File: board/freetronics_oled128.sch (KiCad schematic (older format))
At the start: 42 parts, among them IC1 TPS61040, P1 CONN_10, P2 MICROSD, Q1 2N7002, Q2 2N7002

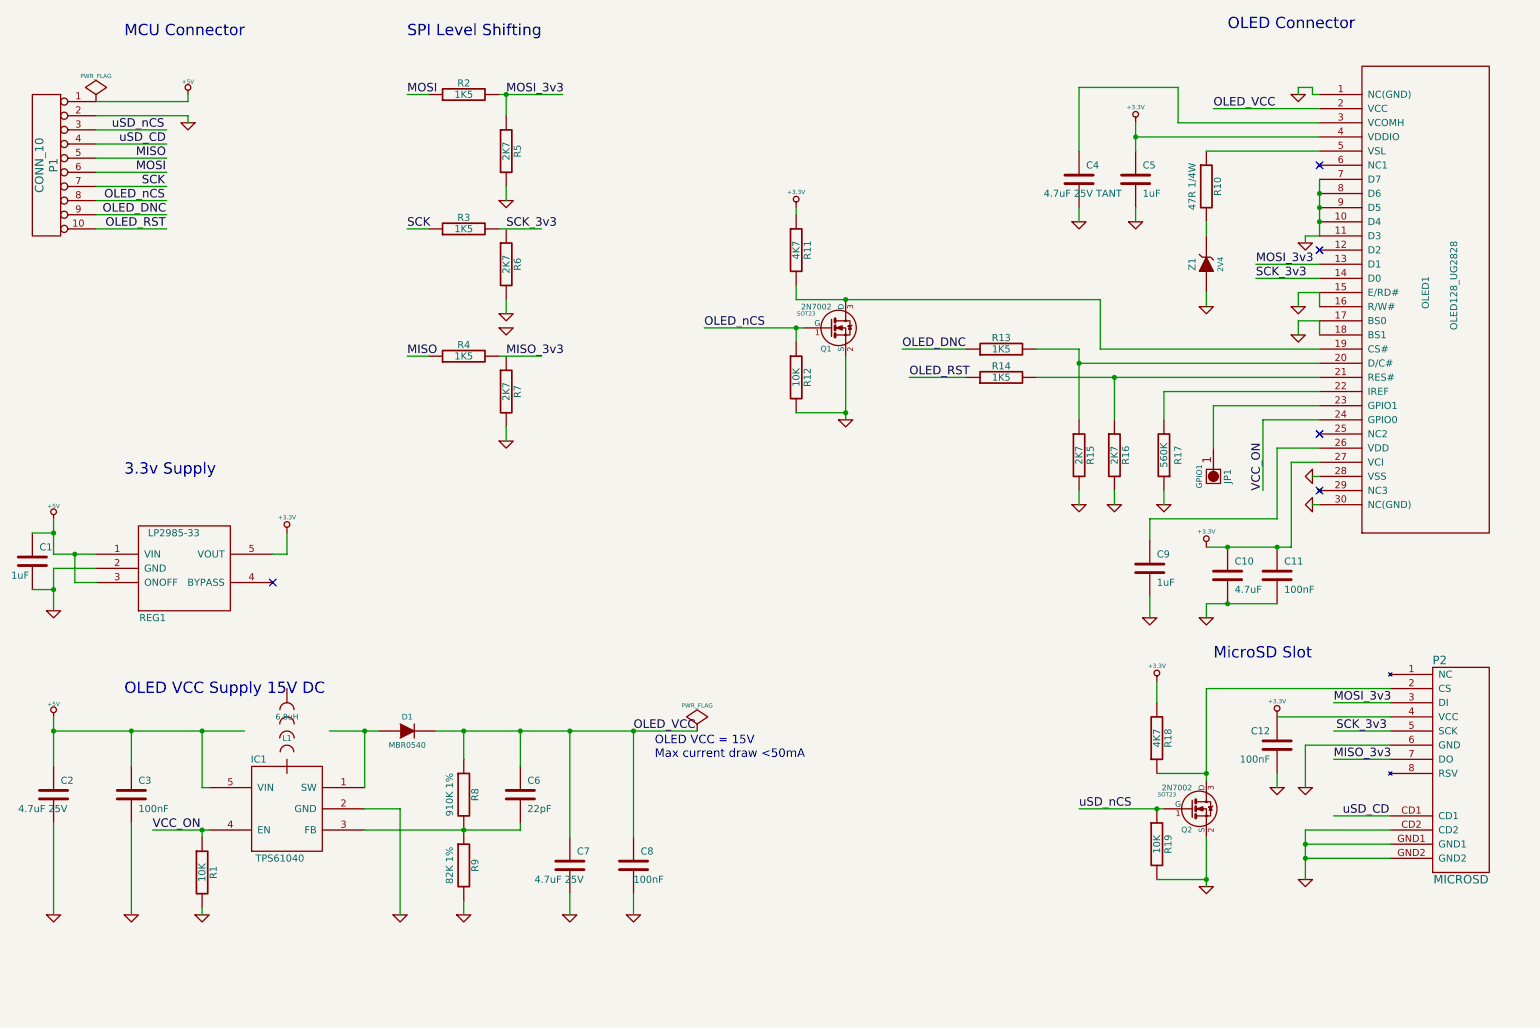
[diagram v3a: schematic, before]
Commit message: Replace ambiguous diode footprint
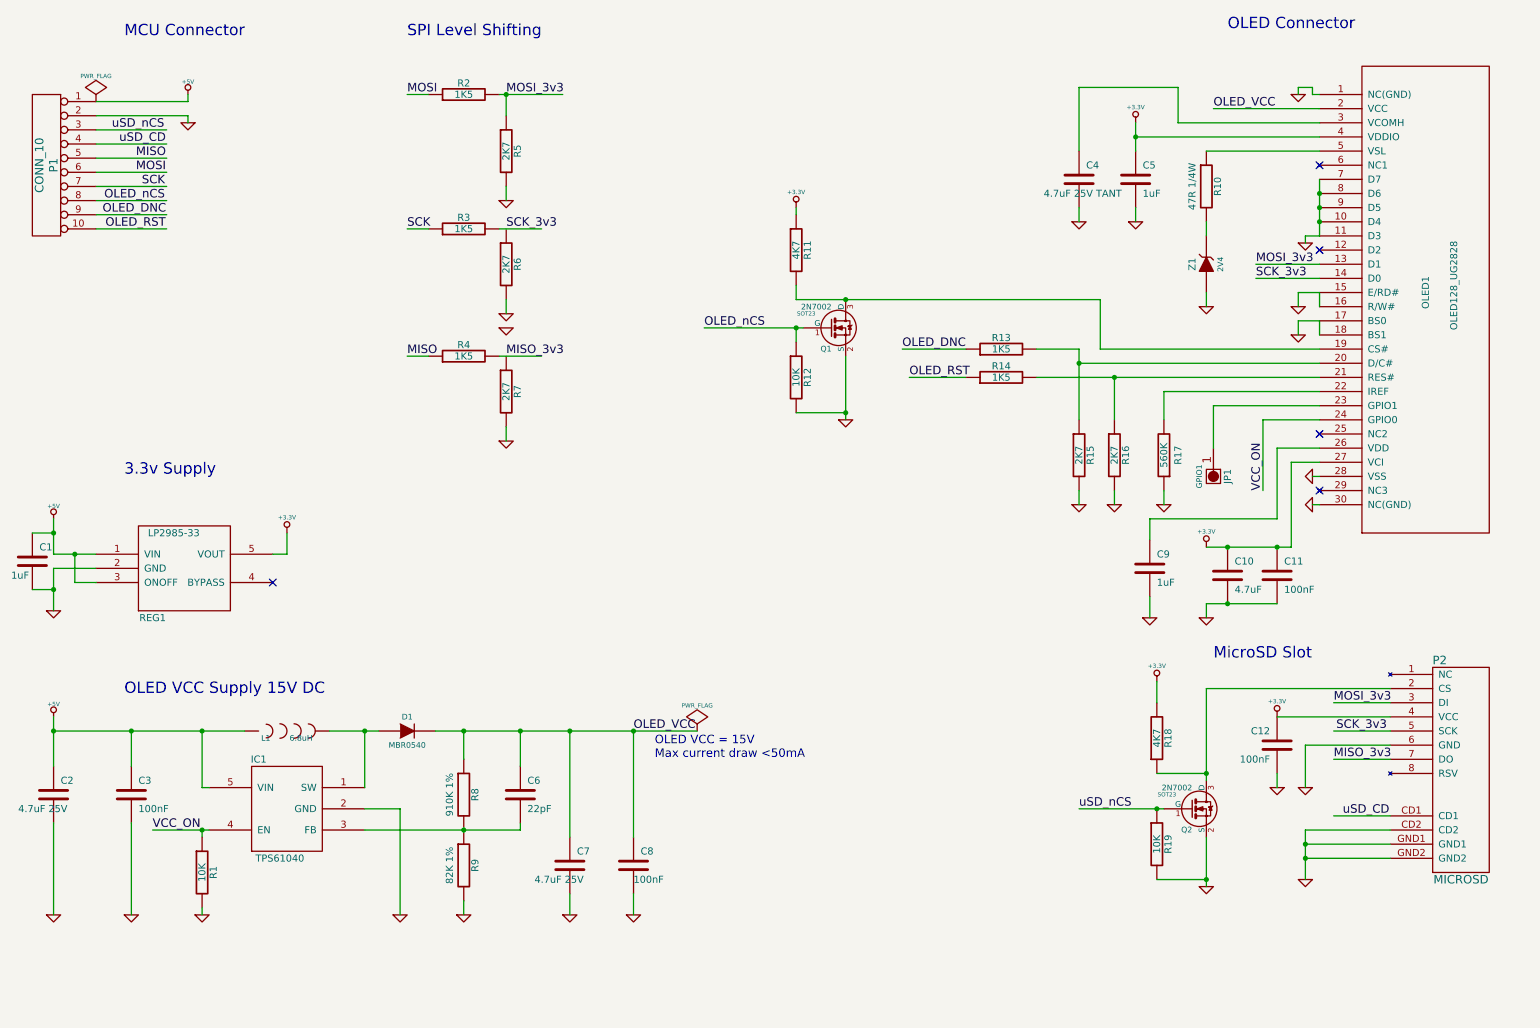
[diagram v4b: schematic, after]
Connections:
- wire segments 170 -> 139
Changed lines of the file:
@@
-EESchema Schematic File Version 2  date Thu 28 Feb 2013 12:36:34 EST
+EESchema Schematic File Version 2  date Tue 19 Mar 2013 09:15:38 EST
+LIBS:freetronics_kicad_sch_lib
 LIBS:power
 LIBS:device
@@
 LIBS:contrib
 LIBS:valves
-LIBS:freetronics_kicad_sch_lib
 LIBS:freetronics_oled128-cache
 EELAYER 25  0
@@
 Sheet 1 1
 Title "Freetronics OLED128              http://www.freetronics.com/oled128"
-Date "28 feb 2013"
+Date "18 mar 2013"
 Rev "0.9"
 Comp "(C)2013 Freetronics Pty Ltd"
@@
 Comment4 ""
 $EndDescr
+$Comp
+L DIODE D1
+U 1 1 514791C6
+P 3250 5650
+F 0 "D1" H 3250 5750 40  0000 C CNN
+F 1 "MBR0540" H 3250 5550 40  0000 C CNN
+	1    3250 5650
+	1    0    0    -1
+$EndComp
 Connection ~ 8250 3150
 Connection ~ 6350 2600
 Wire Wire Line
-	8150 2600 6350 2600
-Wire Wire Line
-	6350 2600 6000 2600
+	8150 2600 6000 2600
 Wire Wire Line
 	6000 2000 6000 1950
@@
 	8700 1350 9700 1350
 Wire Wire Line
-	8400 1350 8400 1450
-Wire Wire Line
-	8400 1450 8400 1550
+	8400 1350 8400 1550
 Connection ~ 8400 1450
 Wire Wire Line
@@
 	6000 2600 6000 2500
 Wire Wire Line
-	6350 3000 6350 3400
-Wire Wire Line
-	6350 3400 6350 3450
+	6350 3000 6350 3450
 Wire Wire Line
 	9700 3250 8600 3250
@@
 	9400 4150 8500 4150
 Wire Wire Line
-	8900 4750 8900 4850
+	8900 4850 8900 4750
 Connection ~ 9400 4350
 Wire Wire Line
 	8500 4700 8500 4850
 Wire Wire Line
-	8900 6000 8900 5950
-Wire Wire Line
-	8900 5950 8900 5350
-Wire Wire Line
-	750  4400 750  4250
-Wire Wire Line
-	750  4250 750  4150
+	8900 6000 8900 5350
+Wire Wire Line
+	750  4150 750  4400
 Connection ~ 8550 6200
 Wire Wire Line
 	1550 1400 1050 1400
 Wire Wire Line
-	8600 6200 8550 6200
-Wire Wire Line
-	8550 6200 8000 6200
+	8600 6200 8000 6200
 Connection ~ 9600 6550
 Wire Wire Line
-	9600 6550 10200 6550
+	10200 6550 9600 6550
 Wire Wire Line
 	9800 6250 10200 6250
@@
 	8550 6700 8900 6700
 Wire Wire Line
-	8900 6400 8900 6700
-Wire Wire Line
-	8900 6700 8900 6750
+	8900 6400 8900 6750
 Connection ~ 8900 6700
 Wire Wire Line
@@
 	9250 2450 9700 2450
 Wire Wire Line
-	4350 1150 3950 1150
-Wire Wire Line
-	3950 1150 3900 1150
+	4350 1150 3900 1150
 Wire Wire Line
 	3950 1300 3950 1150
@@
 	600  4250 750  4250
 Wire Wire Line
-	750  4500 1050 4500
+	1050 4500 750  4500
 Connection ~ 1800 6350
 Wire Wire Line
-	1850 6350 1800 6350
-Wire Wire Line
-	1800 6350 1450 6350
+	1850 6350 1450 6350
 Wire Wire Line
 	1800 6900 1800 6950
 Wire Wire Line
-	750  5900 750  5650
-Wire Wire Line
-	750  5650 750  5550
+	750  5900 750  5550
 Wire Wire Line
 	1300 6300 1300 6950
@@
 	3650 5850 3650 5650
 Wire Wire Line
-	2100 5650 1800 5650
-Wire Wire Line
-	1800 5650 1300 5650
-Wire Wire Line
-	1300 5650 750  5650
+	2100 5650 750  5650
 Connection ~ 3650 6350
 Wire Wire Line
-	4050 6350 4050 6300
+	4050 6300 4050 6350
 Connection ~ 4400 5650
 Wire Wire Line
@@
 	2950 6200 3200 6200
 Wire Wire Line
-	2700 5650 2950 5650
-Wire Wire Line
-	2950 5650 3050 5650
+	2700 5650 3050 5650
 Connection ~ 750  5650
 Wire Wire Line
@@
 	8900 2050 8900 2150
 Wire Wire Line
-	9700 1750 9700 1850
-Wire Wire Line
-	9700 1850 9700 1950
-Wire Wire Line
-	9700 1950 9700 2050
-Wire Wire Line
-	9700 2050 9700 2150
+	9700 1750 9700 2150
 Connection ~ 9700 2050
 Wire Wire Line
@@
 Connection ~ 4850 5650
 Wire Wire Line
-	3450 5650 3650 5650
-Wire Wire Line
-	3650 5650 4050 5650
-Wire Wire Line
-	4050 5650 4400 5650
-Wire Wire Line
-	4400 5650 4850 5650
-Wire Wire Line
-	4850 5650 5300 5650
-Wire Wire Line
-	2950 6350 3650 6350
-Wire Wire Line
-	3650 6350 4050 6350
+	3450 5650 5300 5650
+Wire Wire Line
+	4050 6350 2950 6350
 Wire Wire Line
 	4050 5650 4050 5900
@@
 	1800 6400 1800 6350
 Wire Wire Line
-	900  4600 900  4400
+	900  4400 900  4600
 Wire Wire Line
 	900  4600 1050 4600
 Connection ~ 900  4400
 Wire Wire Line
-	750  4800 750  4650
-Wire Wire Line
-	750  4650 750  4500
+	750  4500 750  4800
 Wire Wire Line
 	600  4650 750  4650
@@
 	8900 5350 10200 5350
 Wire Wire Line
-	9600 6350 10200 6350
-Wire Wire Line
-	9600 6700 9600 6550
-Wire Wire Line
-	9600 6550 9600 6450
-Wire Wire Line
-	9600 6450 9600 6350
+	10200 6350 9600 6350
+Wire Wire Line
+	9600 6350 9600 6700
 Wire Wire Line
 	9600 6450 10200 6450
@@
 	1550 2100 1050 2100
 Wire Wire Line
-	1050 4400 900  4400
-Wire Wire Line
-	900  4400 750  4400
+	750  4400 1050 4400
 Wire Wire Line
 	8550 5300 8550 5450
 Wire Wire Line
-	9500 4350 9500 3750
-Wire Wire Line
-	8900 4350 9050 4350
-Wire Wire Line
-	9050 4350 9400 4350
-Wire Wire Line
-	9400 4350 9500 4350
+	9500 3750 9500 4350
+Wire Wire Line
+	9500 4350 8900 4350
 Connection ~ 9050 4350
 Wire Wire Line
-	9400 4750 9050 4750
-Wire Wire Line
-	9050 4750 8900 4750
+	8900 4750 9400 4750
 Connection ~ 9050 4750
 Wire Wire Line
@@
 	8600 3250 8600 3450
 Wire Wire Line
-	9700 3150 8250 3150
-Wire Wire Line
-	8250 3150 7700 3150
+	9700 3150 7700 3150
 Wire Wire Line
 	8250 3150 8250 3450
@@
 	9700 3050 8000 3050
 Wire Wire Line
-	8000 2950 7700 2950
-Wire Wire Line
-	8000 3450 8000 3050
-Wire Wire Line
-	8000 3050 8000 2950
+	7700 2950 8000 2950
+Wire Wire Line
+	8000 2950 8000 3450
 Connection ~ 6350 3400
 Wire Wire Line
@@
 Connection ~ 6000 2800
 Wire Wire Line
-	5350 2800 6000 2800
-Wire Wire Line
-	6000 2800 6050 2800
+	5350 2800 6050 2800
 Wire Wire Line
 	2300 4400 2400 4400
@@
 $EndComp
 $Comp
-L DIODE D1
-U 1 1 511C32E9
-P 3250 5650
-F 0 "D1" H 3250 5750 40  0000 C CNN
-F 1 "MBR0540" H 3250 5550 40  0000 C CNN
-	1    3250 5650
-	1    0    0    -1
-$EndComp
-$Comp
 L INDUCTOR L1
 U 1 1 511C32D5
 P 2400 5650
-F 0 "L1" V 2350 5650 40  0000 C CNN
-F 1 "6.8uH" V 2500 5650 40  0000 C CNN
+F 0 "L1" H 2250 5600 40  0000 C CNN
+F 1 "6.8uH" H 2500 5600 40  0000 C CNN
 	1    2400 5650
-	0    -1   -1   0
-$EndComp
-$Comp
+	1    0    0    -1
+$EndComp
+$Comp

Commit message: Add optional LEDs and switches on wings
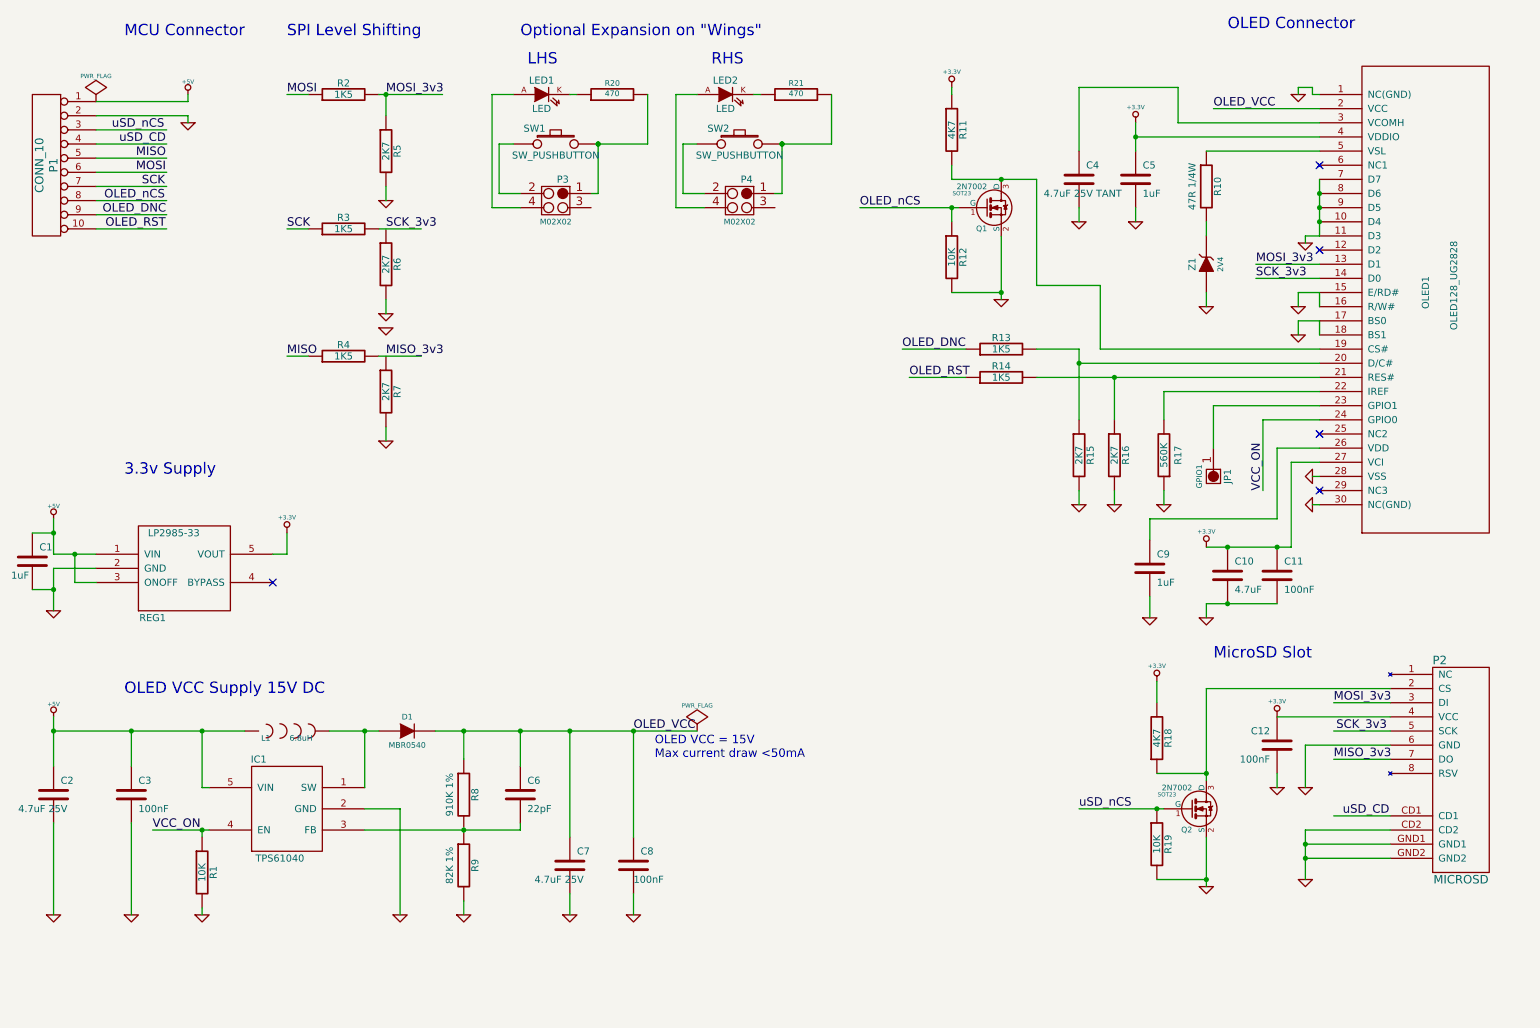
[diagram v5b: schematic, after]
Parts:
- added LED1, LED2: LED, symbol LED
- added P3, P4: M02X02, symbol M02X02
- added R20, R21: 470, ~, symbol R
- added SW1, SW2: SW_PUSHBUTTON, symbol SW_PUSHBUTTON
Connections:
- wire segments 139 -> 163
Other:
- note added: "LHS"
- note added: "Optional Expansion on "Wings""
- note added: "RHS"
- moved on the sheet: Q1, R11, R12, R2, R3, R4, R5, R6, R7
